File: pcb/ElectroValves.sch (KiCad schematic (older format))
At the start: 6 parts, among them U3 TLP240D, U4 TLP240D, U5 TLP240D, U6 TLP240D, U7 TLP240D, U8 TLP240D

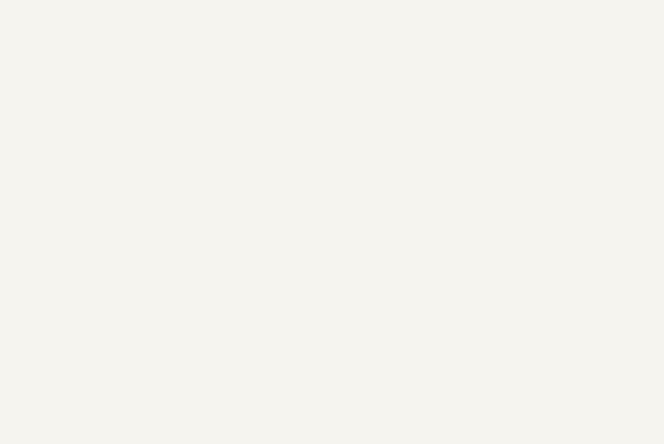
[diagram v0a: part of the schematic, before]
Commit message: AQH3213AX added
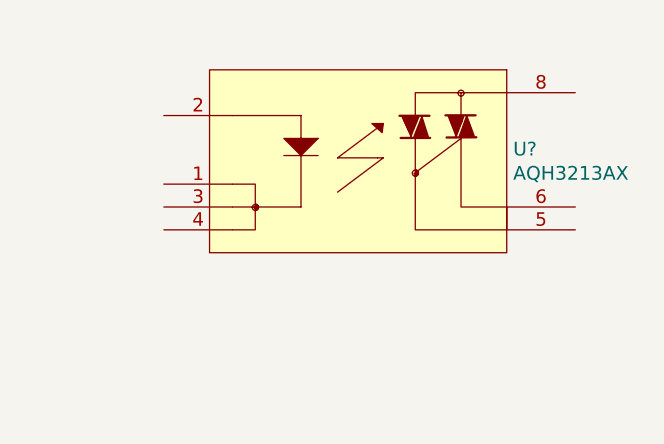
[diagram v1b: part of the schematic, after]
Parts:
- added U?: AQH3213AX, RELAY_AQH_SO8, symbol AQH3213AX:AQH3213AX
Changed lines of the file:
@@
+	1    0    0    -1
+$EndComp
+$Comp
+L AQH3213AX:AQH3213AX U?
+U 1 1 5E8FA1A1
+P 5850 1550
+F 0 "U?" H 7378 1003 60  0000 L CNN
+F 1 "AQH3213AX" H 7378 897 60  0000 L CNN
+F 2 "RELAY_AQH_SO8" H 6750 1790 60  0001 C CNN
+F 3 "" H 5850 1550 60  0000 C CNN
+	1    5850 1550
 	1    0    0    -1
 $EndComp

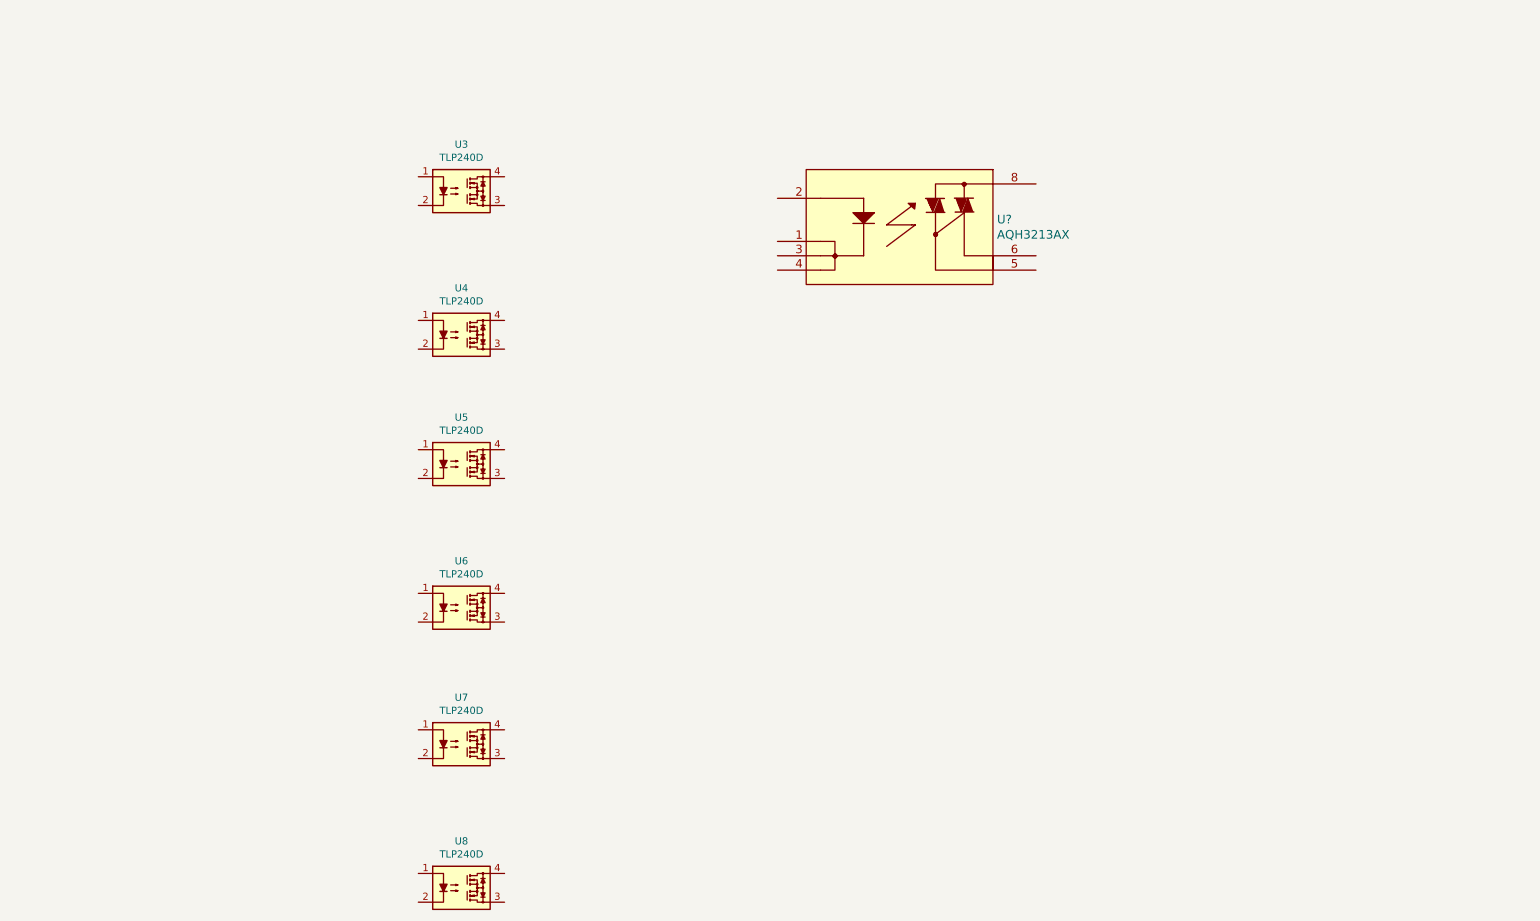
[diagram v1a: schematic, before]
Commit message: added miscellaneous to electro valves sheet
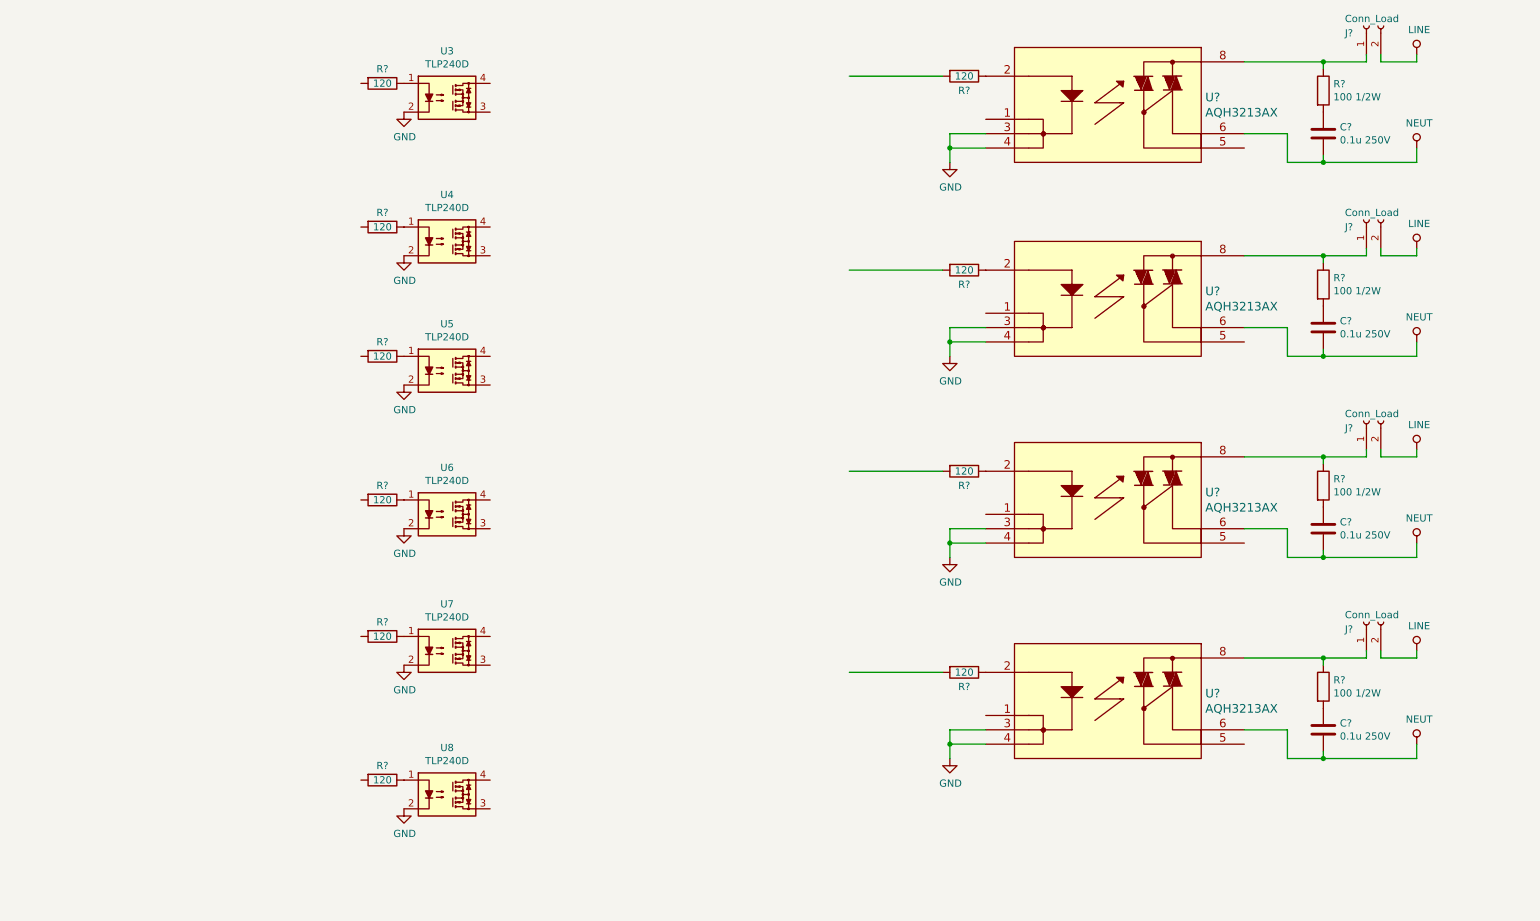
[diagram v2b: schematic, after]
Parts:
- added C? (x4): 0.1u 250V, symbol Device:C
- added J? (x4): Conn_Load, symbol BarrelConnector:Conn_01x02_Female
- added R? (x4): 100 1/2W, symbol Device:R
- added R? (x10): 120, symbol Device:R
- added U? (x3): AQH3213AX, RELAY_AQH_SO8, symbol AQH3213AX:AQH3213AX
- U3, U4, U5, U6, U7, U8: DigiKey (none) -> TLP240D(TP1FCT-ND
- U?: Digikey (none) -> 255-6001-1-ND
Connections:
- net labels added: GND, LINE, NEUT
- wire segments 0 -> 72
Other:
- moved on the sheet: U3, U4, U5, U6, U7, U8, U?

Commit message: AQH3213AX footprint fixed
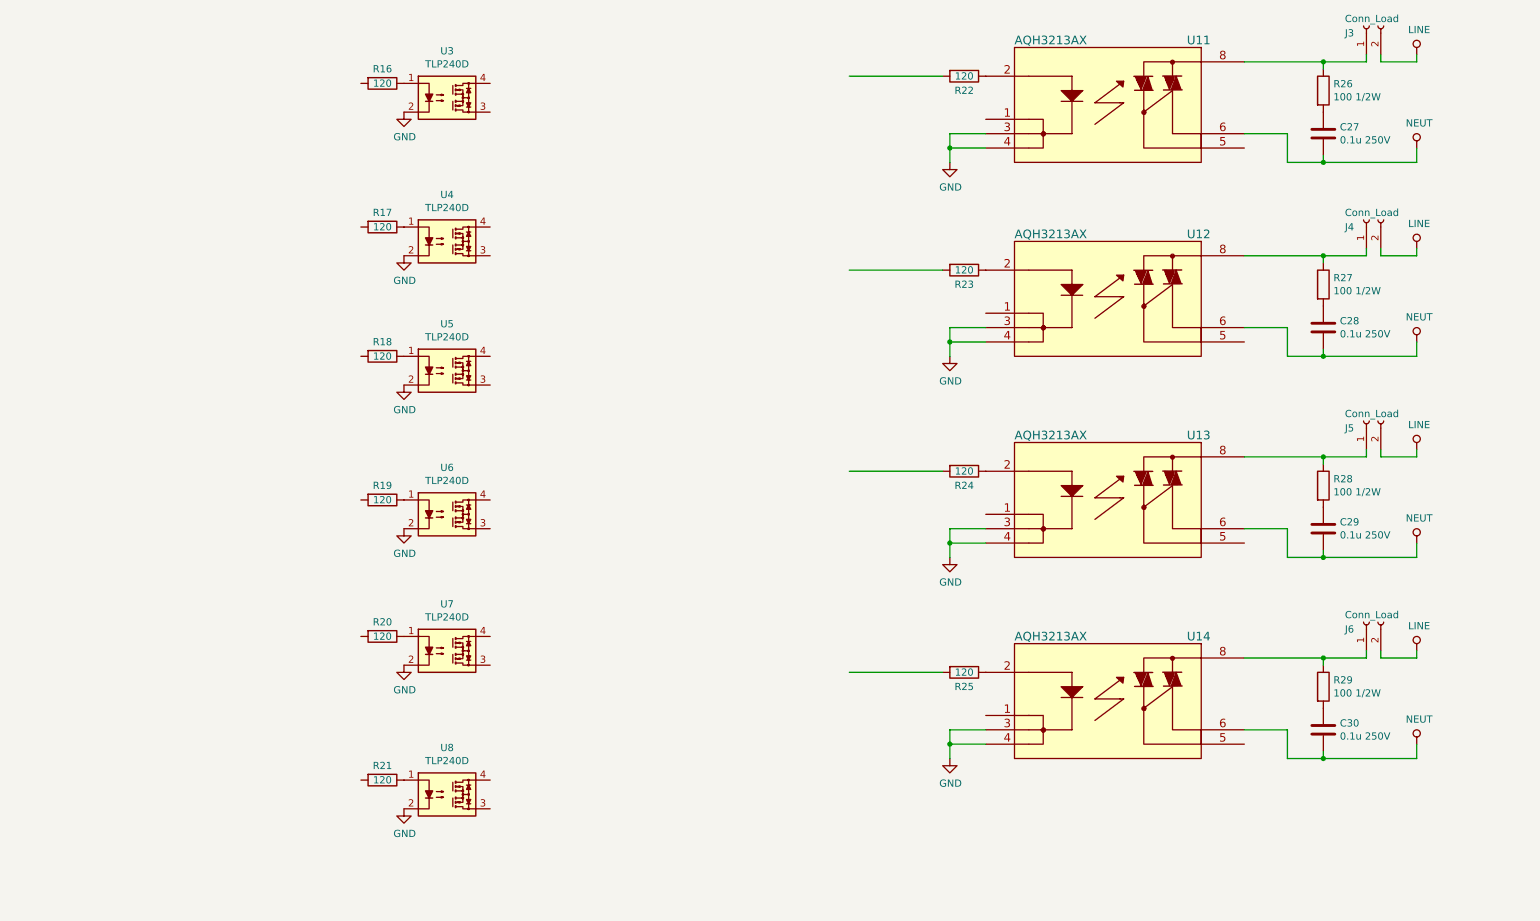
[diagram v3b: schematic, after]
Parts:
- C27, C28, C29, C30: renamed from C?; footprint (none) -> Capacitor_SMD:C_1210_3225Metric
- R26, R27, R28, R29: renamed from R?; footprint (none) -> Resistor_SMD:R_0612_1632Metric; DigiKey 273-KDV12FR120ETCT-ND -> LTR18EZPJ101
- U11, U12, U13, U14: renamed from U?; footprint RELAY_AQH_SO8 -> SMD:AQH3223A
- gave numbers to parts that had none: 14

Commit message: I/O EXPANDER added
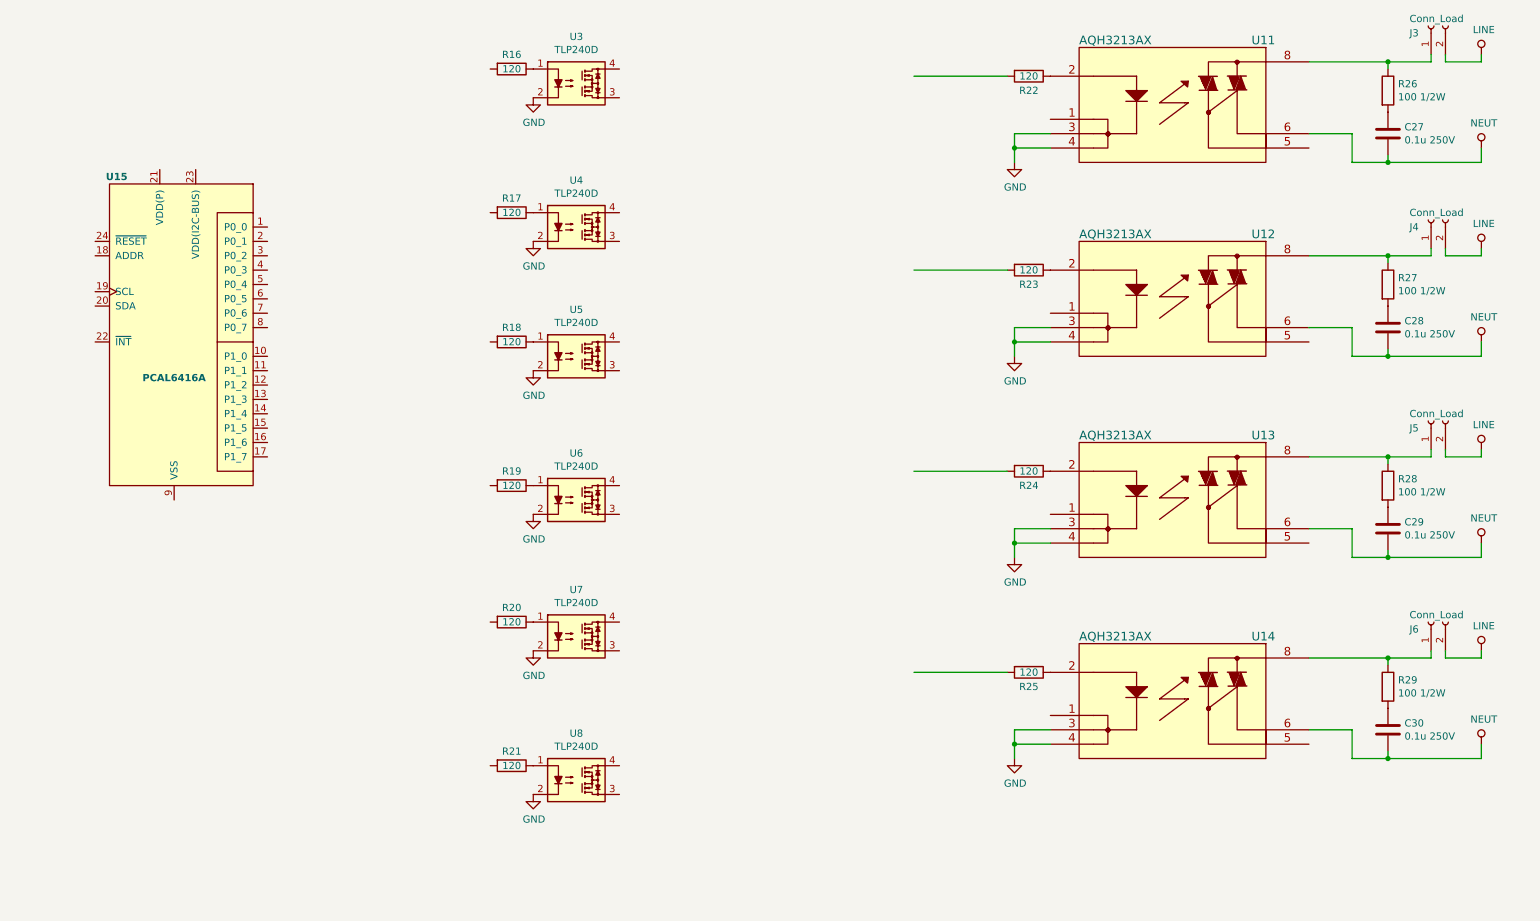
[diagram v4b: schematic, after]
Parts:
- added U15: PCAL6416A, Package_DFN_QFN:QFN-20-1EP_4x4mm_P0.5mm_EP2.5x2.5mm_ThermalVias, symbol PCAL6416AHF:PCAL6416A
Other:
- moved on the sheet: C27, C28, C29, C30, J3, J4, J5, J6, R16, R17, R18, R19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

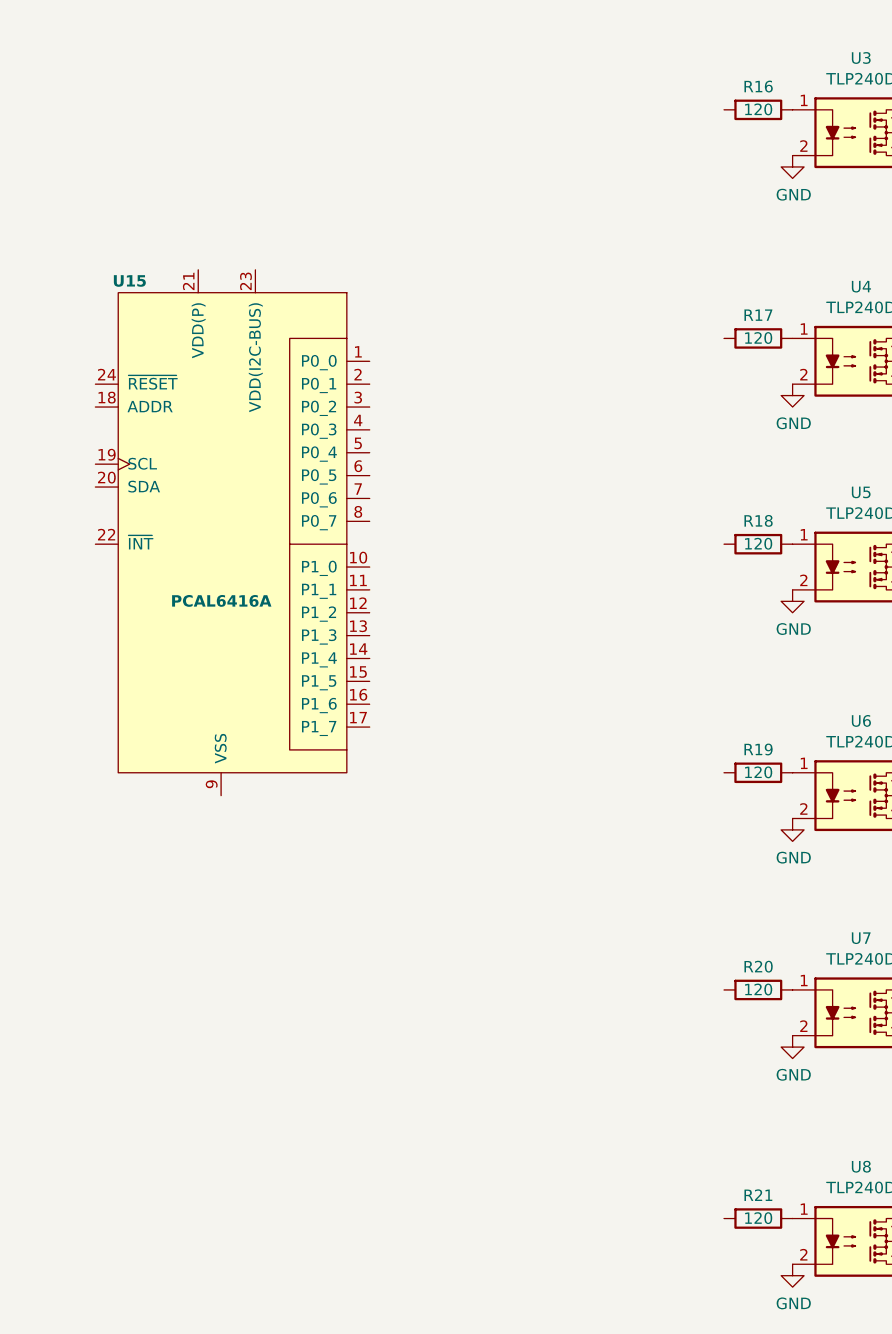
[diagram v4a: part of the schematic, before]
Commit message: connecting relays to the i2c-gpios
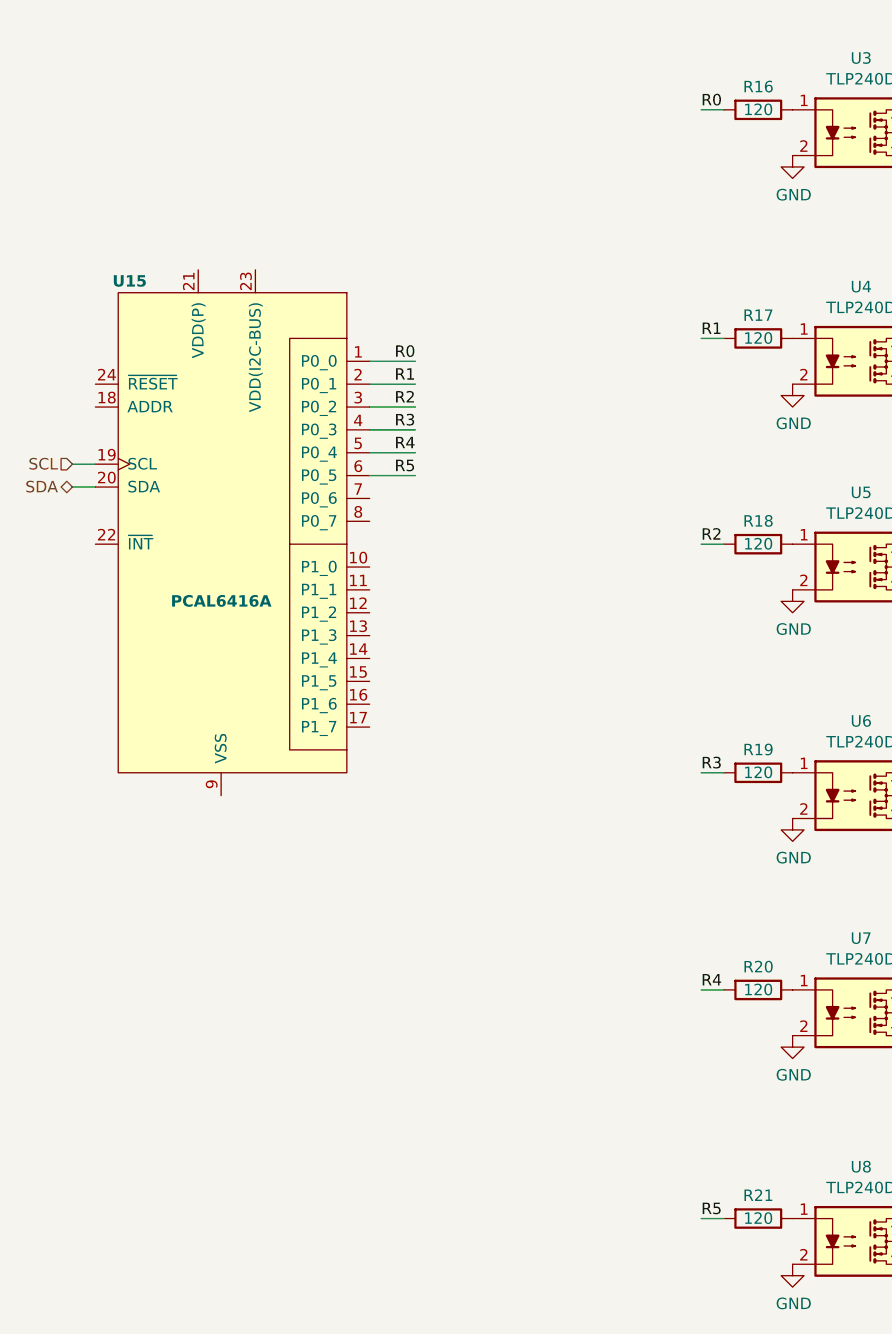
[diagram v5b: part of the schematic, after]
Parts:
- R16, R17, R18, R19, R20, R21: footprint (none) -> Resistor_SMD:R_0402_1005Metric
- U15: footprint Package_DFN_QFN:QFN-20-1EP_4x4mm_P0.5mm_EP2.5x2.5mm_ThermalVias -> Package_DFN_QFN:QFN-20-1EP_4x4mm_P0.5mm_EP2.5x2.5mm
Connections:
- net labels added: R0, R1, R2, R3, R4, R5, SCL, SDA
- wire segments 72 -> 86
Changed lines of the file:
@@
 F 0 "R16" V 3900 1050 50  0000 C CNN
 F 1 "120" V 4000 1050 50  0000 C CNN
-F 2 "" V 3930 1050 50  0001 C CNN
+F 2 "Resistor_SMD:R_0402_1005Metric" V 3930 1050 50  0001 C CNN
 F 3 "~" H 4000 1050 50  0001 C CNN
 	1    4000 1050
@@
 F 0 "R17" V 3900 2050 50  0000 C CNN
 F 1 "120" V 4000 2050 50  0000 C CNN
-F 2 "" V 3930 2050 50  0001 C CNN
+F 2 "Resistor_SMD:R_0402_1005Metric" V 3930 2050 50  0001 C CNN
 F 3 "~" H 4000 2050 50  0001 C CNN
 	1    4000 2050
@@
 F 0 "R18" V 3900 2950 50  0000 C CNN
 F 1 "120" V 4000 2950 50  0000 C CNN
-F 2 "" V 3930 2950 50  0001 C CNN
+F 2 "Resistor_SMD:R_0402_1005Metric" V 3930 2950 50  0001 C CNN
 F 3 "~" H 4000 2950 50  0001 C CNN
 	1    4000 2950
@@
 F 0 "R19" V 3900 3950 50  0000 C CNN
 F 1 "120" V 4000 3950 50  0000 C CNN
-F 2 "" V 3930 3950 50  0001 C CNN
+F 2 "Resistor_SMD:R_0402_1005Metric" V 3930 3950 50  0001 C CNN
 F 3 "~" H 4000 3950 50  0001 C CNN
 	1    4000 3950
@@
 F 0 "R20" V 3900 4900 50  0000 C CNN
 F 1 "120" V 4000 4900 50  0000 C CNN
-F 2 "" V 3930 4900 50  0001 C CNN
+F 2 "Resistor_SMD:R_0402_1005Metric" V 3930 4900 50  0001 C CNN
 F 3 "~" H 4000 4900 50  0001 C CNN
 	1    4000 4900
@@
 F 0 "R21" V 3900 5900 50  0000 C CNN
 F 1 "120" V 4000 5900 50  0000 C CNN
-F 2 "" V 3930 5900 50  0001 C CNN
+F 2 "Resistor_SMD:R_0402_1005Metric" V 3930 5900 50  0001 C CNN
 F 3 "~" H 4000 5900 50  0001 C CNN
 	1    4000 5900
@@
 F 0 "U15" H 1250 4100 50  0000 C CNB
 F 1 "PCAL6416A" H 1650 2700 50  0000 C CNB
-F 2 "Package_DFN_QFN:QFN-20-1EP_4x4mm_P0.5mm_EP2.5x2.5mm_ThermalVias" H 2650 3200 50  0001 C CNN
+F 2 "Package_DFN_QFN:QFN-20-1EP_4x4mm_P0.5mm_EP2.5x2.5mm" H 2650 3200 50  0001 C CNN
 F 3 "" H 2650 3200 50  0001 C CNN
 	1    1650 2950
 	1    0    0    -1
 $EndComp
+Text Label 3750 1050 0    50   ~ 0
+R0
+Wire Wire Line
+	3750 1050 3850 1050
+Text Label 3750 2050 0    50   ~ 0
+R1
+Wire Wire Line
+	3750 2050 3850 2050
+Text Label 3750 2950 0    50   ~ 0
+R2
+Wire Wire Line
+	3750 2950 3850 2950
+Text Label 2500 2150 2    50   ~ 0
+R0
+Wire Wire Line
+	2500 2150 2300 2150
+Text Label 2500 2250 2    50   ~ 0
+R1
+Wire Wire Line
+	2500 2250 2300 2250
+Text Label 2500 2350 2    50   ~ 0
+R2
+Wire Wire Line
+	2500 2350 2300 2350
+Text Label 2500 2450 2    50   ~ 0
+R3
+Wire Wire Line
+	2500 2450 2300 2450
+Text Label 2500 2550 2    50   ~ 0
+R4
+Wire Wire Line
+	2500 2550 2300 2550
+Text Label 2500 2650 2    50   ~ 0
+R5
+Wire Wire Line
+	2500 2650 2300 2650
+Text HLabel 1000 2600 0    50   Input ~ 0
+SCL
+Text HLabel 1000 2700 0    50   BiDi ~ 0
+SDA
+Wire Wire Line
+	1000 2600 1100 2600
+Wire Wire Line
+	1000 2700 1100 2700
+Wire Wire Line
+	3750 5900 3850 5900
+Text Label 3750 5900 0    50   ~ 0
+R5
+Wire Wire Line
+	3750 4900 3850 4900
+Text Label 3750 4900 0    50   ~ 0
+R4
+Wire Wire Line
+	3750 3950 3850 3950
+Text Label 3750 3950 0    50   ~ 0
+R3
 $EndSCHEMATC
